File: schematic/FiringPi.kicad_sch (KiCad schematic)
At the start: 35 parts

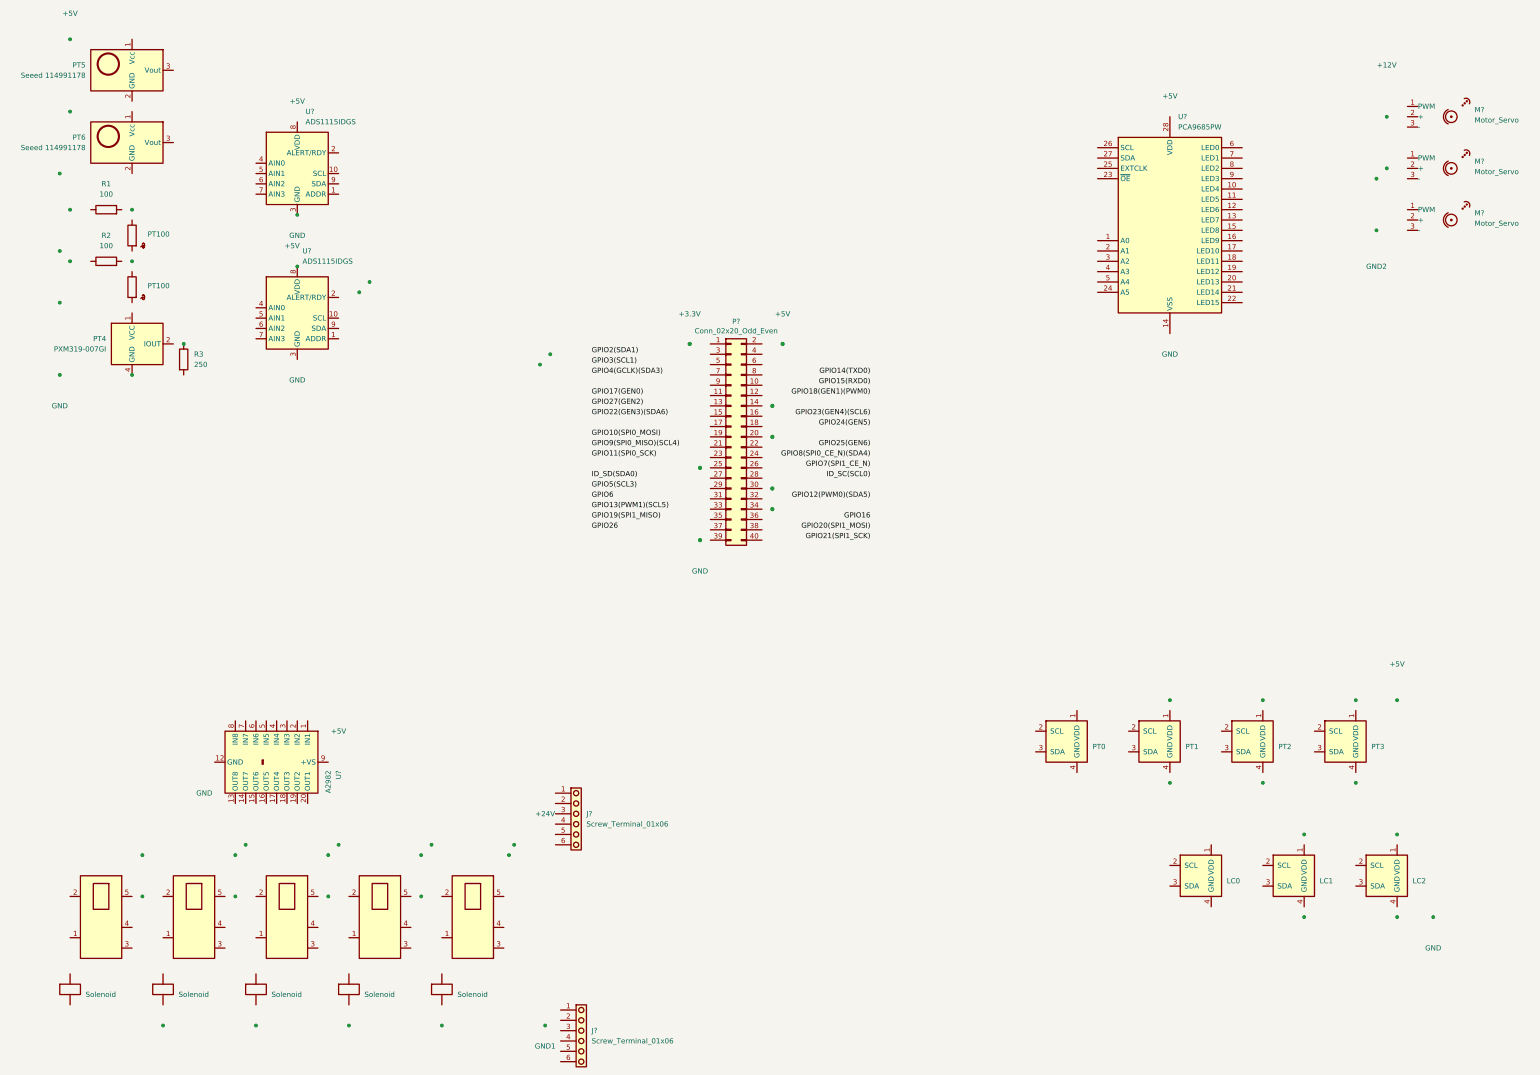
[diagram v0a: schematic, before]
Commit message: Changed stuff over onto buses 1,3,4 because they seem to be the only ones working
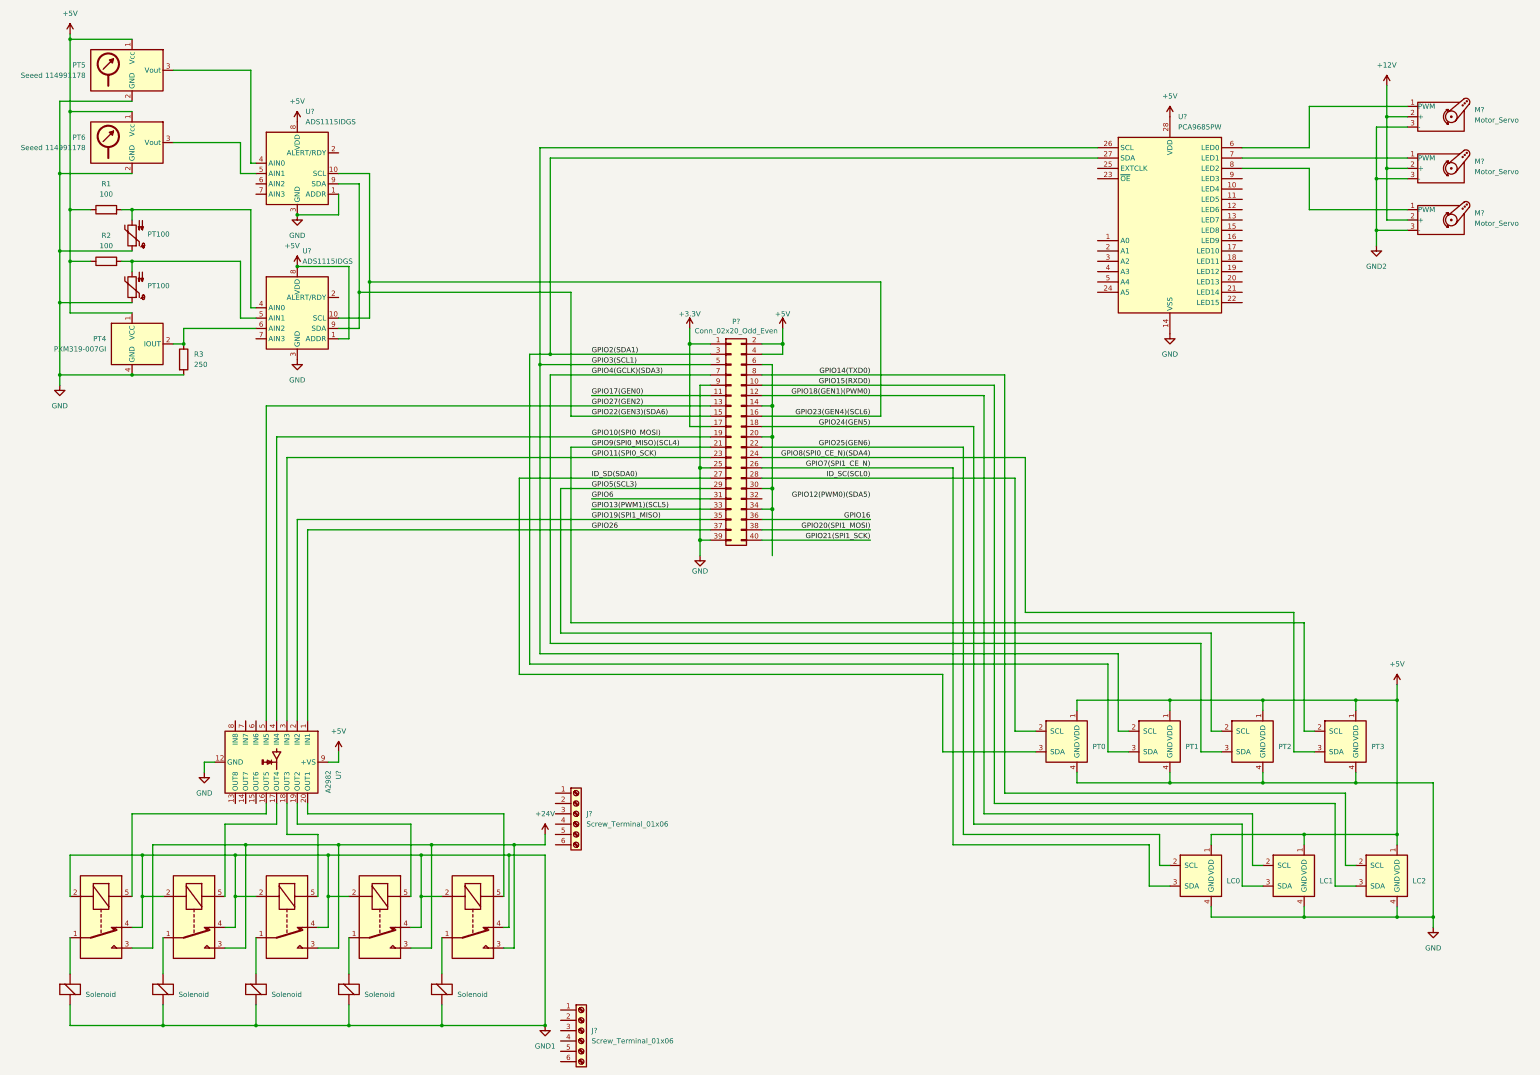
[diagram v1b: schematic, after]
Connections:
- net +12V: now also M?.2 (+), M?.2 (+), M?.2 (+)
- net +24V: now also K?.3, K?.3, K?.3, K?.3, K?.3
- net +3V3: now also P?.1 (Pin_1), P?.17 (Pin_17)
- net +5V: now also P?.2 (Pin_2), P?.4 (Pin_4), PT4.1 (VCC), PT5.1 (Vcc), PT6.1 (Vcc), R1.1, R2.1, U?.1 (ADDR), U?.1 (VDD), U?.1 (VDD), U?.1 (VDD), U?.1 (VDD), U?.1 (VDD), U?.1 (VDD), U?.1 (VDD), U?.9 (+VS)
- net GND: now also P?.25 (Pin_25), P?.39 (Pin_39), P?.9 (Pin_9), PT4.4 (GND), PT5.2 (GND), PT6.2 (GND), R3.2, TH?.1, TH?.1, U?.1 (ADDR), U?.12 (GND), U?.4 (GND), U?.4 (GND), U?.4 (GND), U?.4 (GND), U?.4 (GND), U?.4 (GND), U?.4 (GND), U?.5 (GND), U?.5 (GND), U?.5 (GND), U?.5 (GND), U?.5 (GND), U?.5 (GND), U?.5 (GND)
- net GND1: now also K?.2, K?.2, K?.2, K?.2, K?.2, K?.4, K?.4, K?.4, K?.4, K?.4, L?.2 (+), L?.2 (+), L?.2 (+), L?.2 (+), L?.2 (+)
- net GND2: now also M?.3 (-), M?.3 (-), M?.3 (-)
- net GPIO10(SPI0_MOSI): now also P?.19 (Pin_19), U?.4 (IN4)
- net GPIO11(SPI0_SCK): now also P?.23 (Pin_23), U?.3 (IN3)
- net GPIO13(PWM1)(SCL5): now also P?.33 (Pin_33)
- net GPIO14(TXD0): now also P?.8 (Pin_8), U?.2 (SCL)
- net GPIO15(RXD0): now also P?.10 (Pin_10), U?.3 (SDA)
- net GPIO16: now also P?.36 (Pin_36)
- net GPIO17(GEN0): now also P?.11 (Pin_11)
- net GPIO18(GEN1)(PWM0): now also P?.12 (Pin_12), U?.2 (SCL)
- net GPIO19(SPI1_MISO): now also P?.35 (Pin_35), U?.2 (IN2)
- net GPIO2(SDA1): now also P?.3 (Pin_3), U?.27 (SDA), U?.3 (SDA)
- net GPIO20(SPI1_MOSI): now also P?.38 (Pin_38)
- net GPIO21(SPI1_SCK): now also P?.40 (Pin_40)
- net GPIO22(GEN3)(SDA6): now also P?.15 (Pin_15), U?.9 (SDA), U?.9 (SDA)
- net GPIO23(GEN4)(SCL6): now also P?.16 (Pin_16), U?.10 (SCL), U?.10 (SCL)
- net GPIO24(GEN5): now also P?.18 (Pin_18), U?.3 (SDA)
- net GPIO25(GEN6): now also P?.22 (Pin_22), U?.2 (SCL)
- net GPIO26: now also P?.37 (Pin_37), U?.1 (IN1)
- net GPIO27(GEN2): now also P?.13 (Pin_13), U?.5 (IN5)
- net GPIO3(SCL1): now also P?.5 (Pin_5), U?.2 (SCL), U?.26 (SCL)
- net GPIO4(GCLK)(SDA3): now also P?.7 (Pin_7), U?.3 (SDA)
- net GPIO5(SCL3): now also P?.29 (Pin_29), U?.2 (SCL)
- net GPIO6: now also P?.31 (Pin_31)
- net GPIO7(SPI1_CE_N): now also P?.26 (Pin_26), U?.3 (SDA)
- net GPIO8(SPI0_CE_N)(SDA4): now also P?.24 (Pin_24), U?.3 (SDA)
- net GPIO9(SPI0_MISO)(SCL4): now also P?.21 (Pin_21), U?.2 (SCL)
- net ID_SC(SCL0): now also P?.28 (Pin_28), U?.2 (SCL)
- net ID_SD(SDA0): now also P?.27 (Pin_27), U?.3 (SDA)
- net at R3.1: now also PT4.2 (IOUT), U?.6 (AIN2)
- net at U?.4 (AIN0): now also PT5.3 (Vout)
- net at U?.5 (AIN1): now also PT6.3 (Vout)
- net at L?.1 (-): now also K?.1 (x4)
- net at M?.1 (PWM): now also U?.6 (LED0)
- net at TH?.2: now also R1.2, U?.4 (AIN0)
- net at K?.1: now also L?.1 (-)
- net at K?.5: now also U?.18 (OUT3)
- net at K?.5: now also U?.20 (OUT1)
- net at U?.7 (LED1): now also M?.1 (PWM)
- net at U?.8 (LED2): now also M?.1 (PWM)
- net at TH?.2: now also R2.2, U?.5 (AIN1)
- net at K?.5: now also U?.19 (OUT2)
- net at P?.14 (Pin_14): now also P?.20 (Pin_20), P?.30 (Pin_30), P?.34 (Pin_34), P?.6 (Pin_6)
- net at U?.16 (OUT5): now also K?.5
- net at U?.17 (OUT4): now also K?.5

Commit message: ADC output Added template ADC output to the Display class. Compiles and runs fine, no way to test i2c until the hardware is fixed up.
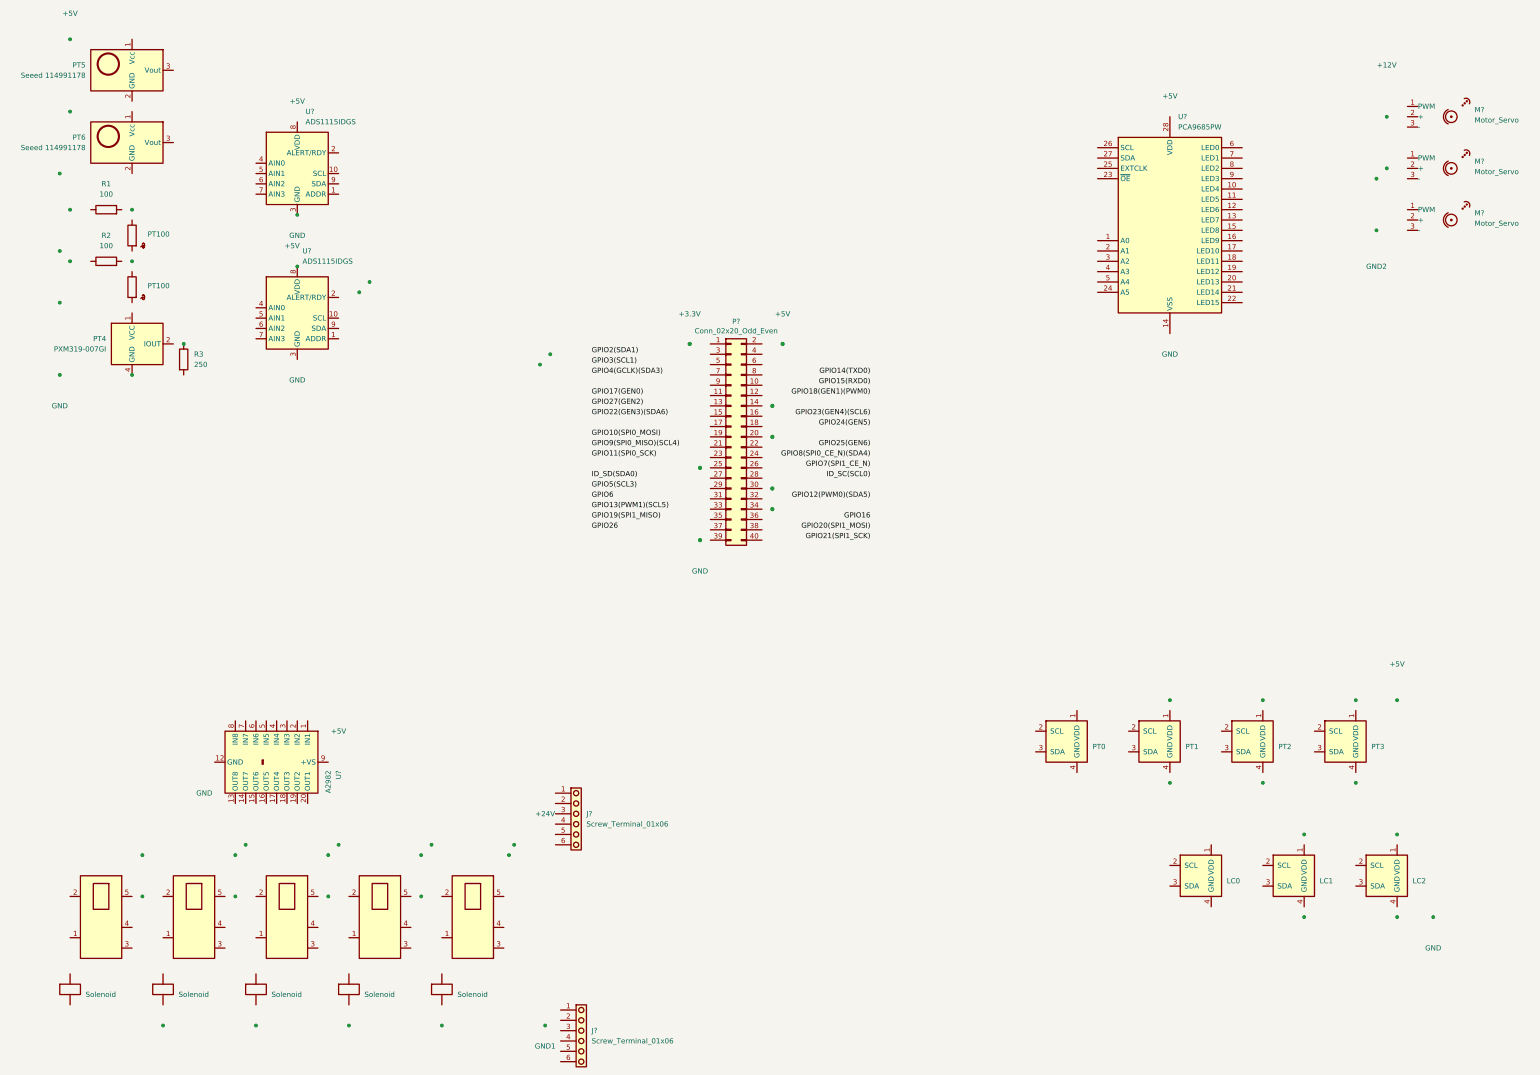
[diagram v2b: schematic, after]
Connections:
- net +12V: no longer M?.2 (+), M?.2 (+), M?.2 (+)
- net +24V: no longer K?.3, K?.3, K?.3, K?.3, K?.3
- net +3V3: no longer P?.1 (Pin_1), P?.17 (Pin_17)
- net +5V: no longer P?.2 (Pin_2), P?.4 (Pin_4), PT4.1 (VCC), PT5.1 (Vcc), PT6.1 (Vcc), R1.1, R2.1, U?.1 (ADDR), U?.1 (VDD), U?.1 (VDD), U?.1 (VDD), U?.1 (VDD), U?.1 (VDD), U?.1 (VDD), U?.1 (VDD), U?.9 (+VS)
- net GND: no longer P?.25 (Pin_25), P?.39 (Pin_39), P?.9 (Pin_9), PT4.4 (GND), PT5.2 (GND), PT6.2 (GND), R3.2, TH?.1, TH?.1, U?.1 (ADDR), U?.12 (GND), U?.4 (GND), U?.4 (GND), U?.4 (GND), U?.4 (GND), U?.4 (GND), U?.4 (GND), U?.4 (GND), U?.5 (GND), U?.5 (GND), U?.5 (GND), U?.5 (GND), U?.5 (GND), U?.5 (GND), U?.5 (GND)
- net GND1: no longer K?.2, K?.2, K?.2, K?.2, K?.2, K?.4, K?.4, K?.4, K?.4, K?.4, L?.2 (+), L?.2 (+), L?.2 (+), L?.2 (+), L?.2 (+)
- net GND2: no longer M?.3 (-), M?.3 (-), M?.3 (-)
- net GPIO10(SPI0_MOSI): no longer P?.19 (Pin_19), U?.4 (IN4)
- net GPIO11(SPI0_SCK): no longer P?.23 (Pin_23), U?.3 (IN3)
- net GPIO13(PWM1)(SCL5): no longer P?.33 (Pin_33)
- net GPIO14(TXD0): no longer P?.8 (Pin_8), U?.2 (SCL)
- net GPIO15(RXD0): no longer P?.10 (Pin_10), U?.3 (SDA)
- net GPIO16: no longer P?.36 (Pin_36)
- net GPIO17(GEN0): no longer P?.11 (Pin_11)
- net GPIO18(GEN1)(PWM0): no longer P?.12 (Pin_12), U?.2 (SCL)
- net GPIO19(SPI1_MISO): no longer P?.35 (Pin_35), U?.2 (IN2)
- net GPIO2(SDA1): no longer P?.3 (Pin_3), U?.27 (SDA), U?.3 (SDA)
- net GPIO20(SPI1_MOSI): no longer P?.38 (Pin_38)
- net GPIO21(SPI1_SCK): no longer P?.40 (Pin_40)
- net GPIO22(GEN3)(SDA6): no longer P?.15 (Pin_15), U?.9 (SDA), U?.9 (SDA)
- net GPIO23(GEN4)(SCL6): no longer P?.16 (Pin_16), U?.10 (SCL), U?.10 (SCL)
- net GPIO24(GEN5): no longer P?.18 (Pin_18), U?.3 (SDA)
- net GPIO25(GEN6): no longer P?.22 (Pin_22), U?.2 (SCL)
- net GPIO26: no longer P?.37 (Pin_37), U?.1 (IN1)
- net GPIO27(GEN2): no longer P?.13 (Pin_13), U?.5 (IN5)
- net GPIO3(SCL1): no longer P?.5 (Pin_5), U?.2 (SCL), U?.26 (SCL)
- net GPIO4(GCLK)(SDA3): no longer P?.7 (Pin_7), U?.3 (SDA)
- net GPIO5(SCL3): no longer P?.29 (Pin_29), U?.2 (SCL)
- net GPIO6: no longer P?.31 (Pin_31)
- net GPIO7(SPI1_CE_N): no longer P?.26 (Pin_26), U?.3 (SDA)
- net GPIO8(SPI0_CE_N)(SDA4): no longer P?.24 (Pin_24), U?.3 (SDA)
- net GPIO9(SPI0_MISO)(SCL4): no longer P?.21 (Pin_21), U?.2 (SCL)
- net ID_SC(SCL0): no longer P?.28 (Pin_28), U?.2 (SCL)
- net ID_SD(SDA0): no longer P?.27 (Pin_27), U?.3 (SDA)
- net at U?.4 (AIN0): no longer PT5.3 (Vout)
- net at U?.5 (AIN1): no longer PT6.3 (Vout)
- net at L?.1 (-): no longer K?.1 (x4)
- net at M?.1 (PWM): no longer U?.6 (LED0)
- net at K?.1: no longer L?.1 (-)
- net at K?.5: no longer U?.18 (OUT3)
- net at K?.5: no longer U?.20 (OUT1)
- net at U?.7 (LED1): no longer M?.1 (PWM)
- net at U?.8 (LED2): no longer M?.1 (PWM)
- net at K?.5: no longer U?.19 (OUT2)
- net at U?.16 (OUT5): no longer K?.5
- net at U?.17 (OUT4): no longer K?.5
- new net: U?.4 (GND), U?.5 (GND) (x7)
- now unconnected: P?.14 (Pin_14), P?.20 (Pin_20), P?.30 (Pin_30), P?.34 (Pin_34), P?.6 (Pin_6), PT4.2 (IOUT), R1.2, R2.2, R3.1, TH?.2, TH?.2, U?.4 (AIN0), U?.5 (AIN1), U?.6 (AIN2)
